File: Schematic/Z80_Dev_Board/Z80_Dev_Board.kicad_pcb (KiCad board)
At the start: 2 copper layers, 101.6 x 83.8 mm, 38 parts, among them J1 MCU Interface, J2 MCU Interface 2, J3 UART B, J4 UART A, J5 Extension Bus, U1 74AC74, U10 SC26C92, U2 74AC04, U3 Z80 CPU, U4 74AC00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

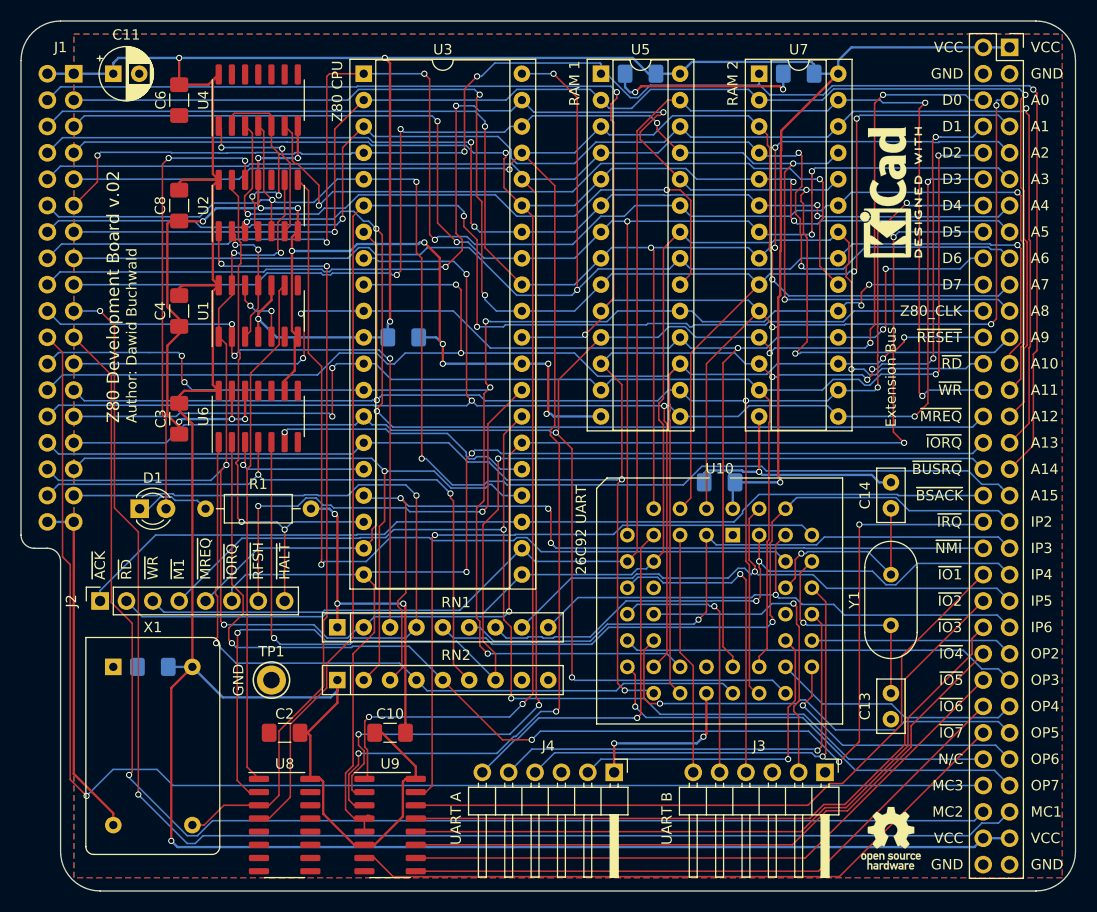
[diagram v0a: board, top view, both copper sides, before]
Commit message: Replaced THT caps/resistors with SMD
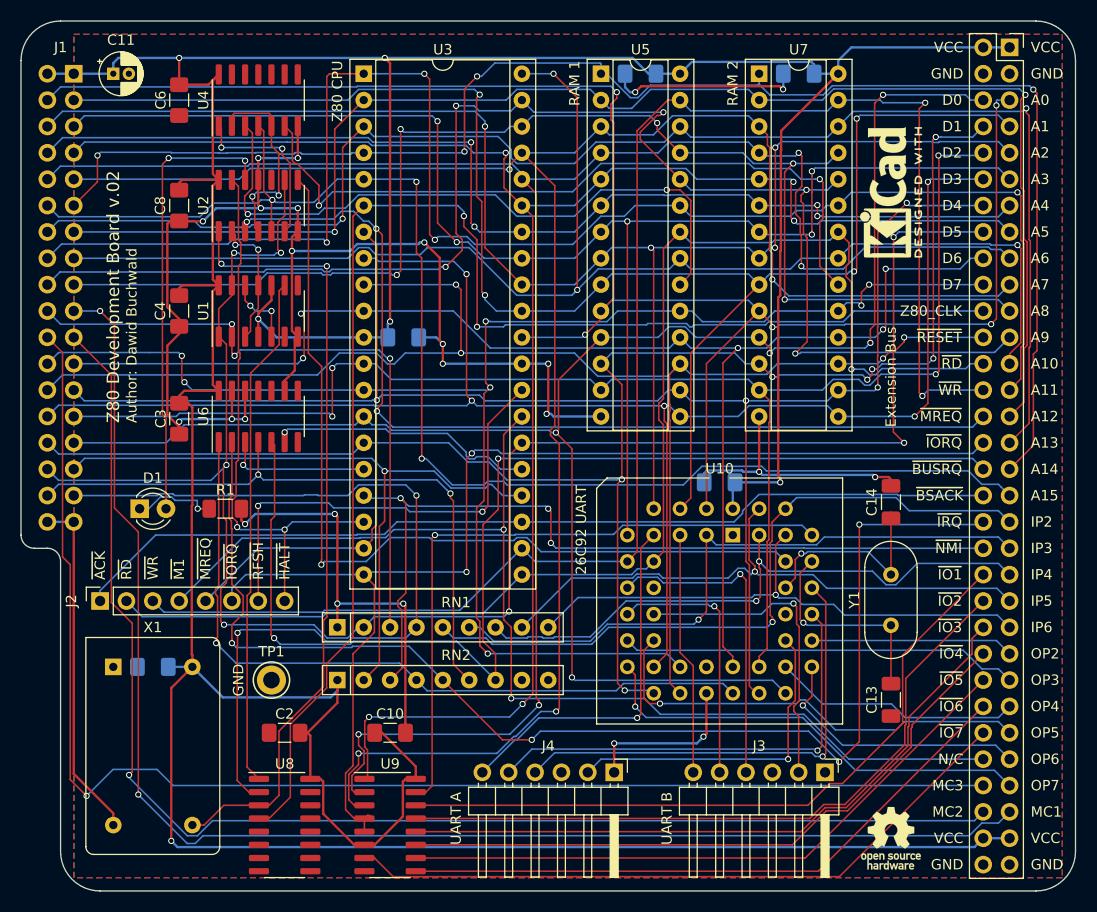
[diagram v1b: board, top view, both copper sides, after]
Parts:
- C11: footprint Capacitor_THT:CP_Radial_D5.0mm_P2.50mm -> Capacitor_THT:CP_Radial_D4.0mm_P1.50mm
- C13, C14: footprint Capacitor_THT:C_Disc_D5.0mm_W2.5mm_P2.50mm -> Capacitor_SMD:C_1206_3216Metric_Pad1.33x1.80mm_HandSolder
- R1: footprint Resistor_THT:R_Axial_DIN0207_L6.3mm_D2.5mm_P10.16mm_Horizontal -> Resistor_SMD:R_1206_3216Metric_Pad1.30x1.75mm_HandSolder
- moved R1 1.90 mm to (108.6, 102.9)
- moved C13 1.87 mm to (172.7, 121.3)
- moved C14 0.59 mm to (172.7, 102.2)
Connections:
- J3 pad 3: (no net) -> Net-(J3-Pad3)
- J4 pad 3: (no net) -> Net-(J4-Pad3)
- RN2 pad 8: (no net) -> Net-(RN2-Pad8)
- RN2 pad 9: (no net) -> Net-(RN2-Pad9)
- U1 pad 6: (no net) -> Net-(U1-Pad6)
- U1 pad 8: (no net) -> Net-(U1-Pad8)
- U10 pad 1: (no net) -> Net-(U10-Pad1)
- U10 pad 12: (no net) -> Net-(U10-Pad12)
- U10 pad 23: (no net) -> Net-(U10-Pad23)
- U10 pad 34: (no net) -> Net-(U10-Pad34)
- U2 pad 10: (no net) -> Net-(U2-Pad10)
- U4 pad 11: (no net) -> Net-(U4-Pad11)
- U4 pad 8: (no net) -> Net-(U4-Pad8)
- U6 pad 11: (no net) -> Net-(U6-Pad11)
- U6 pad 8: (no net) -> Net-(U6-Pad8)
- U8 pad 12: (no net) -> Net-(U8-Pad12)
- U8 pad 7: (no net) -> Net-(U8-Pad7)
- U8 pad 9: (no net) -> Net-(U8-Pad9)
- X1 pad 1: (no net) -> Net-(X1-Pad1)
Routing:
- net GND: track 252.3 -> 260.4 mm, vias 22 -> 24
- net ~UART_IRQ: track 72.0 -> 73.0 mm
- net Net-(C13-Pad2): track 21.6 -> 20.7 mm
- net ~HALT: track 53.1 -> 54.0 mm
- net Net-(D1-Pad1): track 7.28 -> 8.09 mm, vias 0 -> 1
- net +5V: track 426.2 -> 426.8 mm
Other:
- rule pad_to_mask_clearance: 0.05 -> 0

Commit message: Last-minute updates to board layout (and clock toggle schematic)
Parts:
- R1: value 220 -> 470
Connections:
- net Z80_CLK renamed ~Z80_CLK
- U1 pad 11: ~CLK -> CLK
- U1 pad 3: ~CLK -> CLK
- U2 pad 1: CLK -> GND
- U2 pad 2: ~CLK -> Net-(U2-Pad2)
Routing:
- net ~CLK: track 12.8 -> 0.00 mm, vias 2 -> 0
- net GND: track 260.4 -> 262.9 mm, vias 24 -> 25
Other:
- board text added: "~Z80_CLK"
- board text removed: "Z80_CLK"

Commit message: Added QR code for github project
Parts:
- added QR*****: z80_github, Z80:z80_github, B.Cu at (113.0, 128.9)
